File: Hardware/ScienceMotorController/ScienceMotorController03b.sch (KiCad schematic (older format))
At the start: 17 parts, among them U3 VNH5019A_E

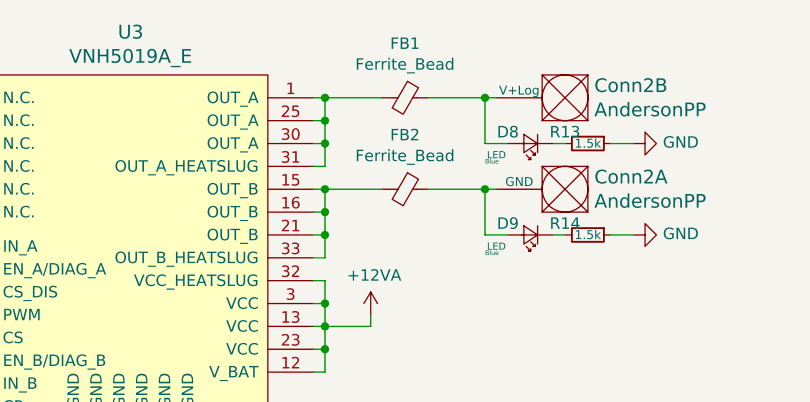
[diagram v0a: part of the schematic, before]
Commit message: finished assigning footprints, generated pcbnew
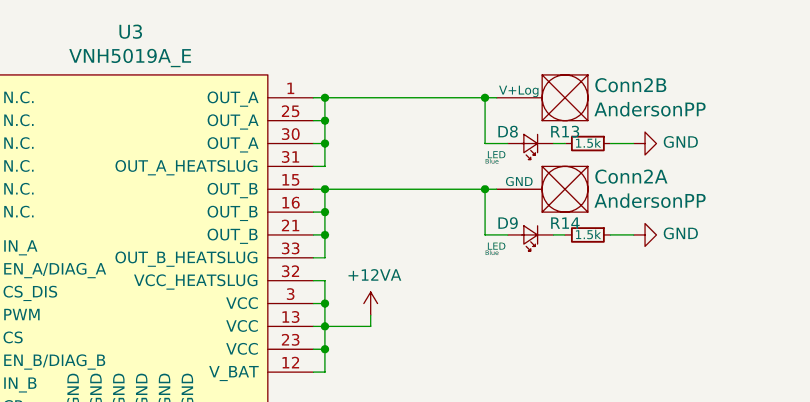
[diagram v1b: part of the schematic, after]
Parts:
- removed FB1, FB2: Ferrite_Bead, symbol Device:Ferrite_Bead_Small
- Conn2: footprint MRDT_Connectors:Anderson_2_Vertical_Sidy_by_Side -> MRDT_Connectors:Anderson_2_Horizontal_Side_by_Side
- U3: footprint (none) -> MRDT_ICs:MultiPowerSO_30
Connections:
- net at Conn2.2 (V+Log), D8.2 (A): now also U3.1 (OUT_A), U3.25 (OUT_A), U3.30 (OUT_A), U3.31 (OUT_A_HEATSLUG)
- net at Conn2.1 (GND), D9.2 (A): now also U3.15 (OUT_B), U3.16 (OUT_B), U3.21 (OUT_B), U3.33 (OUT_B_HEATSLUG)
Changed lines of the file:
@@
 F 0 "U3" H 5700 5937 60  0000 C CNN
 F 1 "VNH5019A_E" H 5700 5831 60  0000 C CNN
-F 2 "" H 5100 5550 60  0001 C CNN
+F 2 "MRDT_ICs:MultiPowerSO_30" H 5100 5550 60  0001 C CNN
 F 3 "" H 5100 5550 60  0001 C CNN
 	1    5100 4250
@@
 F 0 "Conn2" H 7672 3197 60  0000 R CNN
 F 1 "AndersonPP" H 7672 3303 60  0000 R CNN
-F 2 "MRDT_Connectors:Anderson_2_Vertical_Sidy_by_Side" H 7550 2600 60  0001 C CNN
+F 2 "MRDT_Connectors:Anderson_2_Horizontal_Side_by_Side" H 7550 2600 60  0001 C CNN
 F 3 "" H 7550 2600 60  0001 C CNN
 	1    7700 3150
@@
 F 0 "Conn2" H 7672 2797 60  0000 R CNN
 F 1 "AndersonPP" H 7672 2903 60  0000 R CNN
-F 2 "MRDT_Connectors:Anderson_2_Vertical_Sidy_by_Side" H 7550 2200 60  0001 C CNN
+F 2 "MRDT_Connectors:Anderson_2_Horizontal_Side_by_Side" H 7550 2200 60  0001 C CNN
 F 3 "" H 7550 2200 60  0001 C CNN
 	2    7700 2750
@@
 	4900 3900 3950 3900
 Connection ~ 3950 3900
-Wire Wire Line
-	7000 2850 7250 2850
-Wire Wire Line
-	7000 3250 7250 3250
 Wire Wire Line
 	7250 3050 7250 2850
@@
 	1    0    0    -1
 $EndComp
-$Comp
-L Device:Ferrite_Bead_Small FB?
-U 1 1 5F9D0A4B
-P 6900 2850
-AR Path="/5F9082F8/5F9D0A4B" Ref="FB?"  Part="1"
-AR Path="/5F7148FA/5FA34AD5/5F9D0A4B" Ref="FB1"  Part="1"
-F 0 "FB1" V 6663 2850 50  0000 C CNN
-F 1 "Ferrite_Bead" V 6754 2850 50  0000 C CNN
-F 2 "" V 6830 2850 50  0001 C CNN
-F 3 "~" H 6900 2850 50  0001 C CNN
-	1    6900 2850
-	0    1    1    0
-$EndComp
-$Comp
-L Device:Ferrite_Bead_Small FB?
-U 1 1 5F9D10E3
-P 6900 3250
-AR Path="/5F9082F8/5F9D10E3" Ref="FB?"  Part="1"
-AR Path="/5F7148FA/5FA34AD5/5F9D10E3" Ref="FB2"  Part="1"
-F 0 "FB2" V 6663 3250 50  0000 C CNN
-F 1 "Ferrite_Bead" V 6754 3250 50  0000 C CNN
-F 2 "" V 6830 3250 50  0001 C CNN
-F 3 "~" H 6900 3250 50  0001 C CNN
-	1    6900 3250
-	0    1    1    0
-$EndComp
-Wire Wire Line
-	6800 2850 6550 2850
 Connection ~ 6550 2850
-Wire Wire Line
-	6800 3250 6550 3250
 Connection ~ 6550 3250
 Text HLabel 4450 3500 0    50   Input ~ 0
@@
 Text Notes 7250 3550 0    20   ~ 0
 Blue
+Wire Wire Line
+	6550 3250 7250 3250
+Wire Wire Line
+	6550 2850 7250 2850
 $EndSCHEMATC

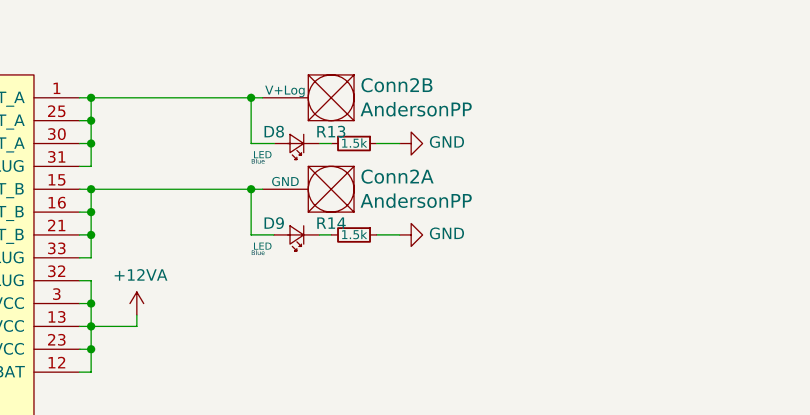
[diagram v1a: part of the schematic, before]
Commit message: running traces
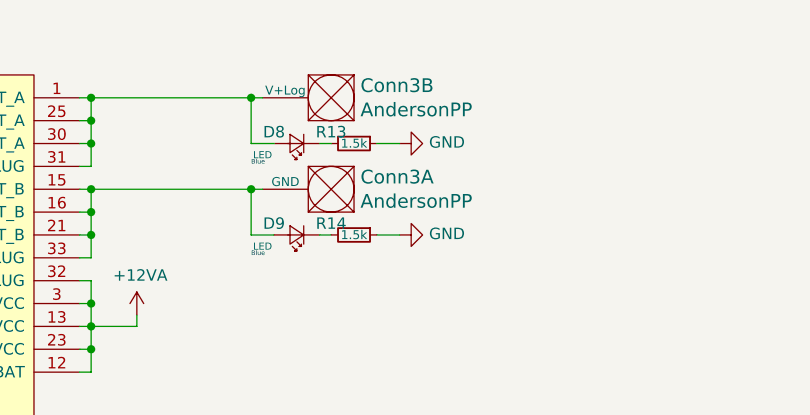
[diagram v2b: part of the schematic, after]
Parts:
- renumbered Conn2 to Conn3
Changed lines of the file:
@@
 AR Path="/5F7D111E/5FA36344/5FA5B7FC" Ref="Conn?"  Part="1"
 AR Path="/5F9082F8/5FA5B7FC" Ref="Conn?"  Part="1"
-AR Path="/5F7148FA/5FA34AD5/5FA5B7FC" Ref="Conn2"  Part="1"
-F 0 "Conn2" H 7672 3197 60  0000 R CNN
+AR Path="/5F7148FA/5FA34AD5/5FA5B7FC" Ref="Conn3"  Part="1"
+F 0 "Conn3" H 7672 3197 60  0000 R CNN
 F 1 "AndersonPP" H 7672 3303 60  0000 R CNN
 F 2 "MRDT_Connectors:Anderson_2_Horizontal_Side_by_Side" H 7550 2600 60  0001 C CNN
@@
 AR Path="/5F7D111E/5FA36344/5FA5B802" Ref="Conn?"  Part="2"
 AR Path="/5F9082F8/5FA5B802" Ref="Conn?"  Part="2"
-AR Path="/5F7148FA/5FA34AD5/5FA5B802" Ref="Conn2"  Part="2"
-F 0 "Conn2" H 7672 2797 60  0000 R CNN
+AR Path="/5F7148FA/5FA34AD5/5FA5B802" Ref="Conn3"  Part="2"
+F 0 "Conn3" H 7672 2797 60  0000 R CNN
 F 1 "AndersonPP" H 7672 2903 60  0000 R CNN
 F 2 "MRDT_Connectors:Anderson_2_Horizontal_Side_by_Side" H 7550 2200 60  0001 C CNN
